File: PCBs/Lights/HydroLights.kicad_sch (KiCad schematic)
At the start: 12 parts, among them U1 Solder_Pad, U10 Solder_Pad, U11 Solder_Pad, U2 Solder_Pad, U3 158303250A (Daylight) 3v 65mA, U4 150283HS73103 (Red) 2.6v 150mA, U5 158303250A (Daylight) 3v 65mA, U6 150283BS73103 (Blue) 3.5v 150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, U7 158303250A (Daylight) 3v 65mA, U8 150283GS73103 (Green) 3.5v 15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

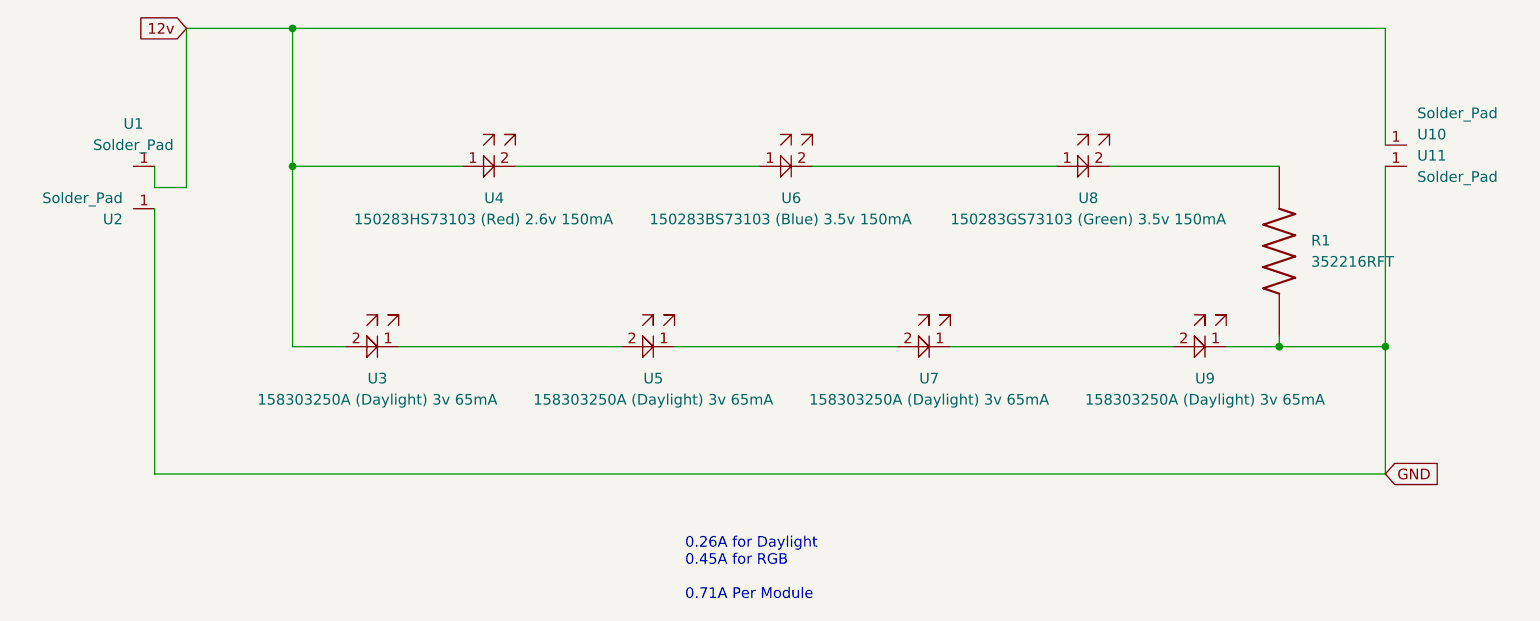
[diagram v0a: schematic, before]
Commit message: Remove steppers, add OLED
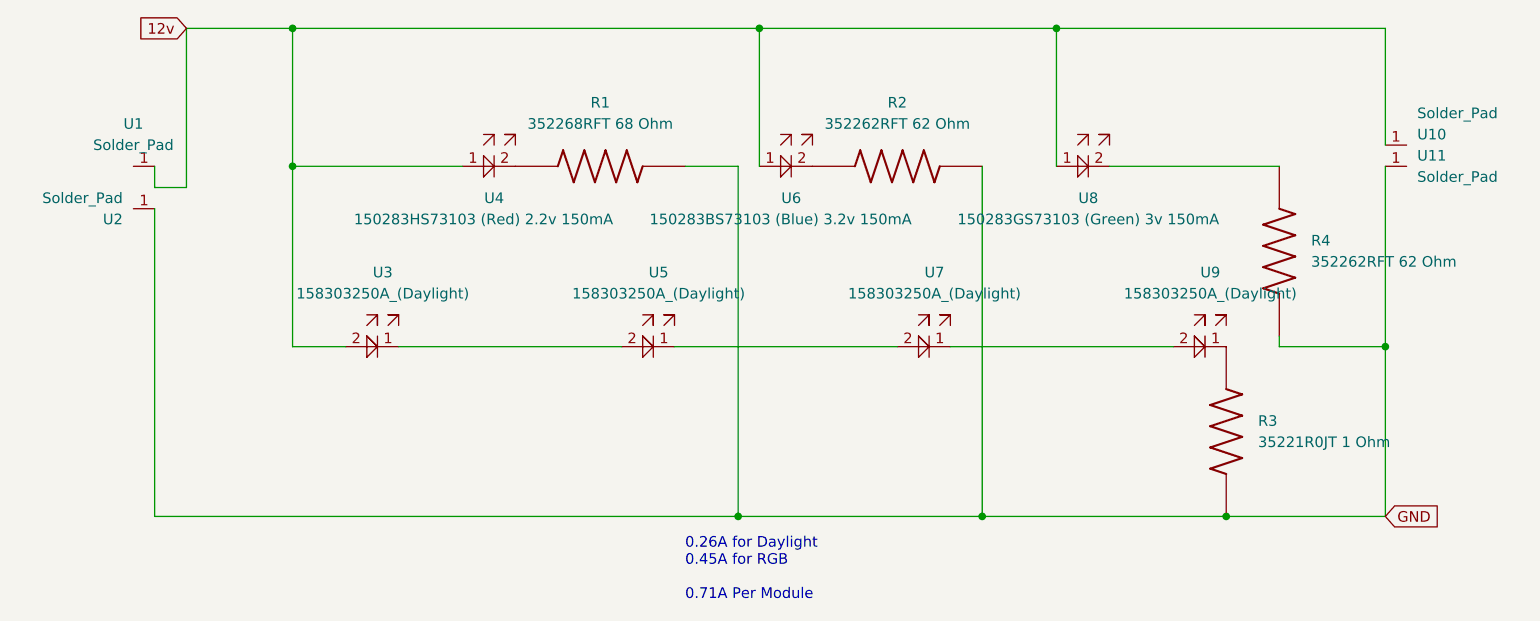
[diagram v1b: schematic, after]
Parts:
- removed R1: 352216RFT, SnapEDA Library:RESC6332X120N, symbol 352216RFT:352216RFT
- added R1: 352268RFT 68 Ohm, SnapEDA Library:RESC6332X120N, symbol 352268RFT:352268RFT
- added R2, R4: 352262RFT 62 Ohm, SnapEDA Library:RESC6332X120N, symbol 352262RFT:352262RFT
- added R3: 35221R0JT 1 Ohm, SnapEDA Library:RESC6332X120N, symbol 35221R0JT:35221R0JT
- U3, U5, U7, U9: value 158303250A (Daylight) 3v 65mA -> 158303250A_(Daylight)
- U4: value 150283HS73103 (Red) 2.6v 150mA -> 150283HS73103 (Red) 2.2v 150mA
- U6: value 150283BS73103 (Blue) 3.5v 150mA -> 150283BS73103 (Blue) 3.2v 150mA
- U8: value 150283GS73103 (Green) 3.5v 150mA -> 150283GS73103 (Green) 3v 150mA
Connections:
- net 12v: now also U6.1, U8.1
- net GND: now also R1.2, R2.2, R3.1, R4.2; no longer U9.1
- net at U6.2: now also R2.1; no longer U8.1
- net at U8.2: now also R4.1
- net at U4.2: now also R1.1; no longer U6.1
- new net: R3.2, U9.1
